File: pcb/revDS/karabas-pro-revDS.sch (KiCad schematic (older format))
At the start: 212 parts, among them CON1 CF-CARD, CON2 SD, CON3 VGA, CON4 Joystick, CON5 Keyboard, CON6 Mouse, CON7 Audio, CON8 12V, CON9 MicroSD', J1 Floppy, J10 Ext Joystick, J2 FPGA JTAG, J3 Floppy, J4 uBus, J5 AVR JTAG, J6 AVR UART, J7 ESP-BUS, J8 Tape In, J9 Tape Out, Q1 BC856, Q2 BC548, SW1 SW_Push, SW2 SW_Push, SW4 SW_SPST, U1 EP4CE10E22C8N, U10 ESP-12E, U11 TDA1543, U12 AMS1117-3.3, U13 AMS1117-2.5, U14 AMS1117-1.2, U15 LM2596S-5, U16 LM311, U17 74LS06, U18 74LS38, U2 CY62167EV30LL, U3 W25Q16, U3''1 W25Q16, U4 EPM3128ATC100-10N, U5 ATMEGA328-AU, U6 MB8877A, U7 TXB0104PW, U8 TXB0104PW, U9 DS1307Z+, X1 SG-7050CAN, Y1 32768Hz, Y2 16MHz

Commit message: Fixed beeper
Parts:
- Q2: value BC548 -> BC847; symbol Transistor_BJT:BC548 -> Transistor_BJT:BC847
- R48: value 1k -> 15k*
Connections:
- net VCC3_3: now also Q2.3 (C); no longer Q2.1 (C)
- net at D10.1 (K), R48.1: now also Q2.1 (B); no longer Q2.2 (B)
- net at LS1.1 (-): now also Q2.2 (E); no longer Q2.3 (E)
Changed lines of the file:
@@
 L5
 $Comp
-L Transistor_BJT:BC548 Q2
+L Transistor_BJT:BC847 Q2
 U 1 1 60A22677
 P 8100 8700
 F 0 "Q2" H 8291 8746 50  0000 L CNN
-F 1 "BC548" H 8291 8655 50  0000 L CNN
+F 1 "BC847" H 8291 8655 50  0000 L CNN
 F 2 "Package_TO_SOT_SMD:SOT-23" H 8300 8625 50  0001 L CIN
 F 3 "https://www.onsemi.com/pub/Collateral/BC550-D.pdf" H 8100 8700 50  0001 L CNN
@@
 U 1 1 608D1972
 P 7850 8400
-F 0 "R48" V 8057 8400 50  0000 C CNN
-F 1 "1k" V 7966 8400 50  0000 C CNN
+F 0 "R48" V 8050 8350 50  0000 C CNN
+F 1 "15k*" V 7950 8350 50  0000 C CNN
 F 2 "Resistor_SMD:R_0805_2012Metric_Pad1.20x1.40mm_HandSolder" V 7780 8400 50  0001 C CNN
 F 3 "~" H 7850 8400 50  0001 C CNN
@@
 Wire Wire Line
 	7850 8150 7900 8150
+Connection ~ 7900 8150
 Wire Bus Line
 	4850 6350 5350 6350
@@
 Wire Bus Line
 	6500 700  6500 12500
-Connection ~ 7900 8150
 $EndSCHEMATC

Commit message: Updated gerbers, schematics for revDS
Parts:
- R80: value 10k -> 5k1
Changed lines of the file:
@@
 P 2300 14050
 F 0 "R80" V 2507 14050 50  0000 C CNN
-F 1 "10k" V 2416 14050 50  0000 C CNN
+F 1 "5k1" V 2416 14050 50  0000 C CNN
 F 2 "Resistor_SMD:R_0805_2012Metric_Pad1.20x1.40mm_HandSolder" V 2230 14050 50  0001 C CNN
 F 3 "~" H 2300 14050 50  0001 C CNN

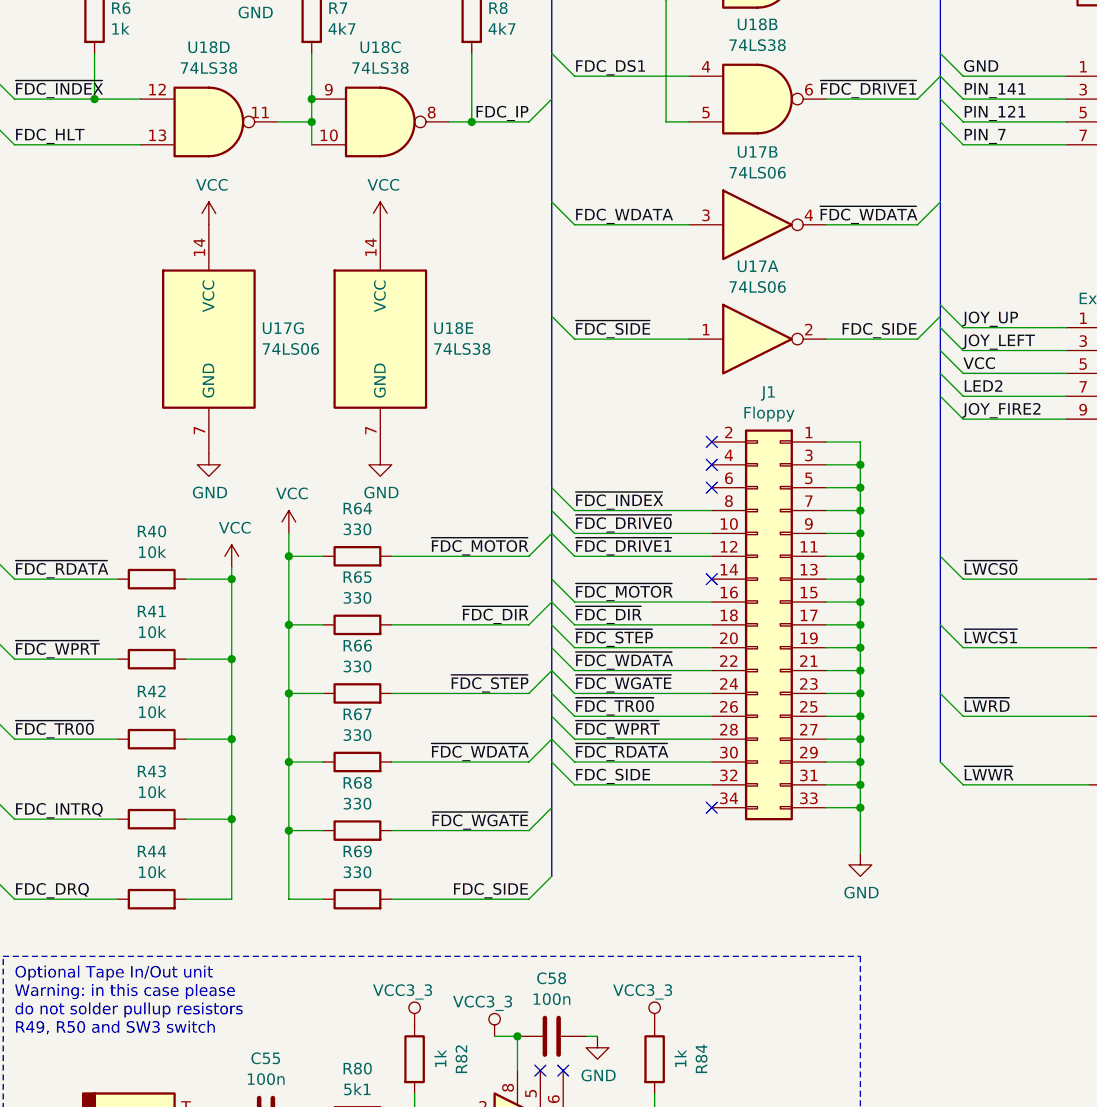
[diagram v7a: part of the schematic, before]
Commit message: Updated schematics: added note about optional terminators
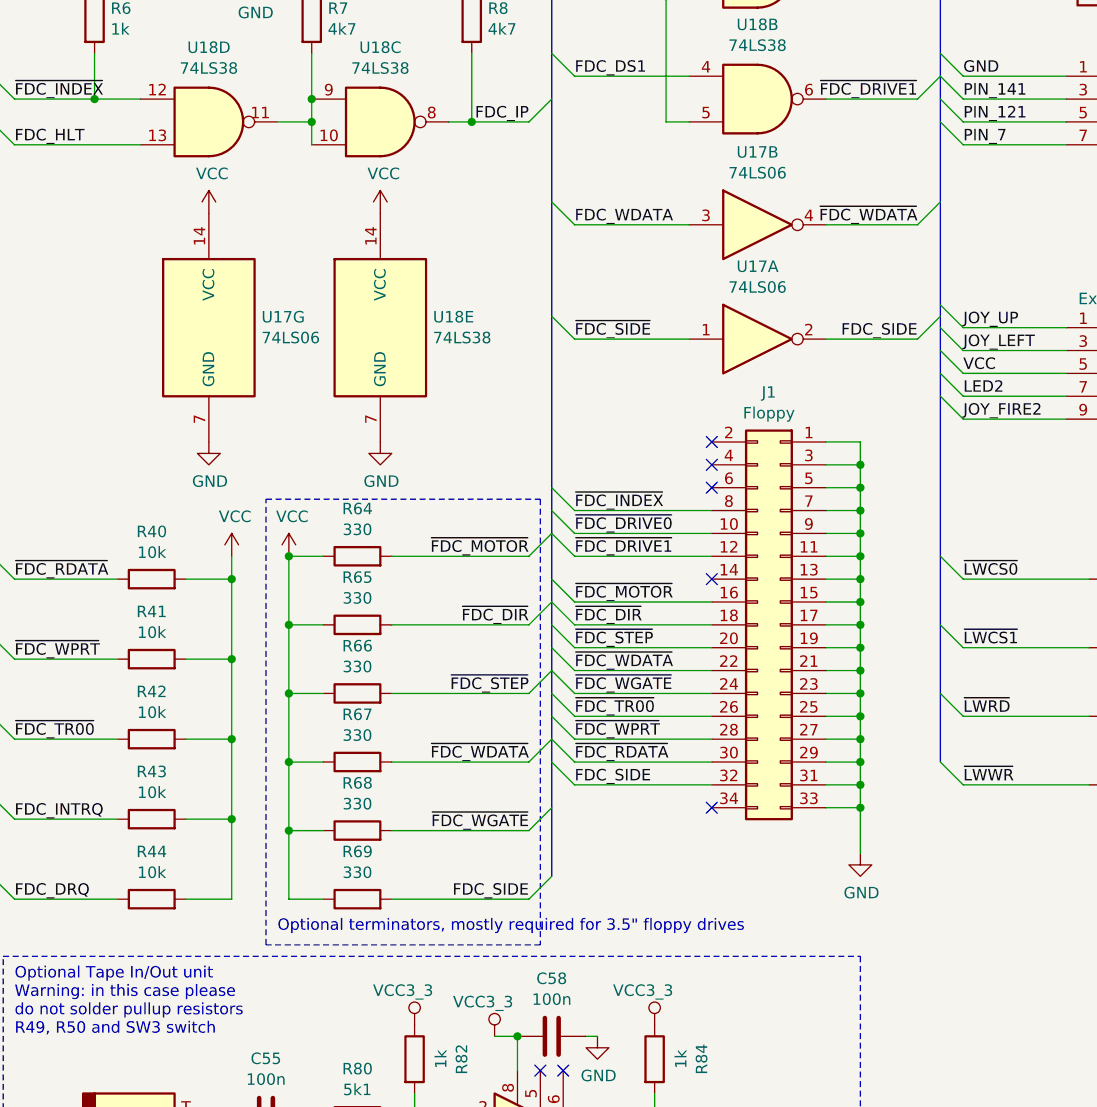
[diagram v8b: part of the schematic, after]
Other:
- note added: "Optional terminators, mostly required for 3.5" floppy drives"
- moved on the sheet: U17G, U18E
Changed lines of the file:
@@
 L 74xx:74LS06 U17
 U 7 1 5EDDEA20
-P 1650 10650
-F 0 "U17" H 1880 10696 50  0000 L CNN
-F 1 "74LS06" H 1880 10605 50  0000 L CNN
-F 2 "Package_DIP:DIP-14_W7.62mm" H 1650 10650 50  0001 C CNN
-F 3 "http://www.ti.com/lit/gpn/sn74LS06" H 1650 10650 50  0001 C CNN
-	7    1650 10650
+P 1650 10600
+F 0 "U17" H 1880 10646 50  0000 L CNN
+F 1 "74LS06" H 1880 10555 50  0000 L CNN
+F 2 "Package_DIP:DIP-14_W7.62mm" H 1650 10600 50  0001 C CNN
+F 3 "http://www.ti.com/lit/gpn/sn74LS06" H 1650 10600 50  0001 C CNN
+	7    1650 10600
 	1    0    0    -1
 $EndComp
@@
 L 74xx:74LS38 U18
 U 5 1 5EDE4EC9
-P 2400 10650
-F 0 "U18" H 2630 10696 50  0000 L CNN
-F 1 "74LS38" H 2630 10605 50  0000 L CNN
-F 2 "Package_DIP:DIP-14_W7.62mm" H 2400 10650 50  0001 C CNN
-F 3 "http://www.ti.com/lit/gpn/sn74LS38" H 2400 10650 50  0001 C CNN
-	5    2400 10650
+P 2400 10600
+F 0 "U18" H 2630 10646 50  0000 L CNN
+F 1 "74LS38" H 2630 10555 50  0000 L CNN
+F 2 "Package_DIP:DIP-14_W7.62mm" H 2400 10600 50  0001 C CNN
+F 3 "http://www.ti.com/lit/gpn/sn74LS38" H 2400 10600 50  0001 C CNN
+	5    2400 10600
 	1    0    0    -1
 $EndComp
@@
 L power:VCC #PWR0111
 U 1 1 609C2FC1
-P 1650 10150
-F 0 "#PWR0111" H 1650 10000 50  0001 C CNN
-F 1 "VCC" H 1665 10323 50  0000 C CNN
-F 2 "" H 1650 10150 50  0001 C CNN
-F 3 "" H 1650 10150 50  0001 C CNN
-	1    1650 10150
+P 1650 10100
+F 0 "#PWR0111" H 1650 9950 50  0001 C CNN
+F 1 "VCC" H 1665 10273 50  0000 C CNN
+F 2 "" H 1650 10100 50  0001 C CNN
+F 3 "" H 1650 10100 50  0001 C CNN
+	1    1650 10100
 	1    0    0    -1
 $EndComp
@@
 L power:VCC #PWR0112
 U 1 1 609C446B
-P 2400 10150
-F 0 "#PWR0112" H 2400 10000 50  0001 C CNN
-F 1 "VCC" H 2415 10323 50  0000 C CNN
-F 2 "" H 2400 10150 50  0001 C CNN
-F 3 "" H 2400 10150 50  0001 C CNN
-	1    2400 10150
+P 2400 10100
+F 0 "#PWR0112" H 2400 9950 50  0001 C CNN
+F 1 "VCC" H 2415 10273 50  0000 C CNN
+F 2 "" H 2400 10100 50  0001 C CNN
+F 3 "" H 2400 10100 50  0001 C CNN
+	1    2400 10100
 	1    0    0    -1
 $EndComp
@@
 L power:GND #PWR0113
 U 1 1 609C4B89
-P 1650 11150
-F 0 "#PWR0113" H 1650 10900 50  0001 C CNN
-F 1 "GND" H 1655 10977 50  0000 C CNN
-F 2 "" H 1650 11150 50  0001 C CNN
-F 3 "" H 1650 11150 50  0001 C CNN
-	1    1650 11150
+P 1650 11100
+F 0 "#PWR0113" H 1650 10850 50  0001 C CNN
+F 1 "GND" H 1655 10927 50  0000 C CNN
+F 2 "" H 1650 11100 50  0001 C CNN
+F 3 "" H 1650 11100 50  0001 C CNN
+	1    1650 11100
 	1    0    0    -1
 $EndComp
@@
 L power:GND #PWR0114
 U 1 1 609C5169
-P 2400 11150
-F 0 "#PWR0114" H 2400 10900 50  0001 C CNN
-F 1 "GND" H 2405 10977 50  0000 C CNN
-F 2 "" H 2400 11150 50  0001 C CNN
-F 3 "" H 2400 11150 50  0001 C CNN
-	1    2400 11150
+P 2400 11100
+F 0 "#PWR0114" H 2400 10850 50  0001 C CNN
+F 1 "GND" H 2405 10927 50  0000 C CNN
+F 2 "" H 2400 11100 50  0001 C CNN
+F 3 "" H 2400 11100 50  0001 C CNN
+	1    2400 11100
 	1    0    0    -1
 $EndComp
@@
 L power:VCC #PWR0177
 U 1 1 5F2C0719
-P 1750 11650
-F 0 "#PWR0177" H 1750 11500 50  0001 C CNN
-F 1 "VCC" H 1765 11823 50  0000 C CNN
-F 2 "" H 1750 11650 50  0001 C CNN
-F 3 "" H 1750 11650 50  0001 C CNN
-	1    1750 11650
+P 1750 11600
+F 0 "#PWR0177" H 1750 11450 50  0001 C CNN
+F 1 "VCC" H 1765 11773 50  0000 C CNN
+F 2 "" H 1750 11600 50  0001 C CNN
+F 3 "" H 1750 11600 50  0001 C CNN
+	1    1750 11600
 	1    0    0    -1
 $EndComp
 Wire Wire Line
-	1750 11650 1750 11700
+	1750 11600 1750 11700
 Wire Wire Line
 	1750 13100 1550 13100
@@
 L power:VCC #PWR016
 U 1 1 6258E15E
-P 2000 11500
-F 0 "#PWR016" H 2000 11350 50  0001 C CNN
-F 1 "VCC" H 2015 11673 50  0000 C CNN
-F 2 "" H 2000 11500 50  0001 C CNN
-F 3 "" H 2000 11500 50  0001 C CNN
-	1    2000 11500
+P 2000 11600
+F 0 "#PWR016" H 2000 11450 50  0001 C CNN
+F 1 "VCC" H 2015 11773 50  0000 C CNN
+F 2 "" H 2000 11600 50  0001 C CNN
+F 3 "" H 2000 11600 50  0001 C CNN
+	1    2000 11600
 	1    0    0    -1
 $EndComp
-Wire Wire Line
-	2000 11500 2000 11600
 Connection ~ 2000 11600
 Text Label 8850 10050 0    50   ~ 0
@@
 	7850 8150 7900 8150
 Connection ~ 7900 8150
+Wire Notes Line
+	3100 11350 3100 13300
+Wire Notes Line
+	3100 13300 1900 13300
+Wire Notes Line
+	1900 13300 1900 11350
+Wire Notes Line
+	1900 11350 3100 11350
 Wire Bus Line
 	4850 6350 5350 6350
@@
 Wire Bus Line
 	6500 700  6500 12500
+Text Notes 1950 13250 0    50   ~ 0
+Optional terminators, mostly required for 3.5" floppy drives
 $EndSCHEMATC
